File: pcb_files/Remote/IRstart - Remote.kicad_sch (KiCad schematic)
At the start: 32 parts, among them Q1 2N7002, Q2 2N7002, SW1 SW_DIP_x02, SW2 SW_DIP_x02, SW3 SW_DPDT_x2, U2 AP1117-33

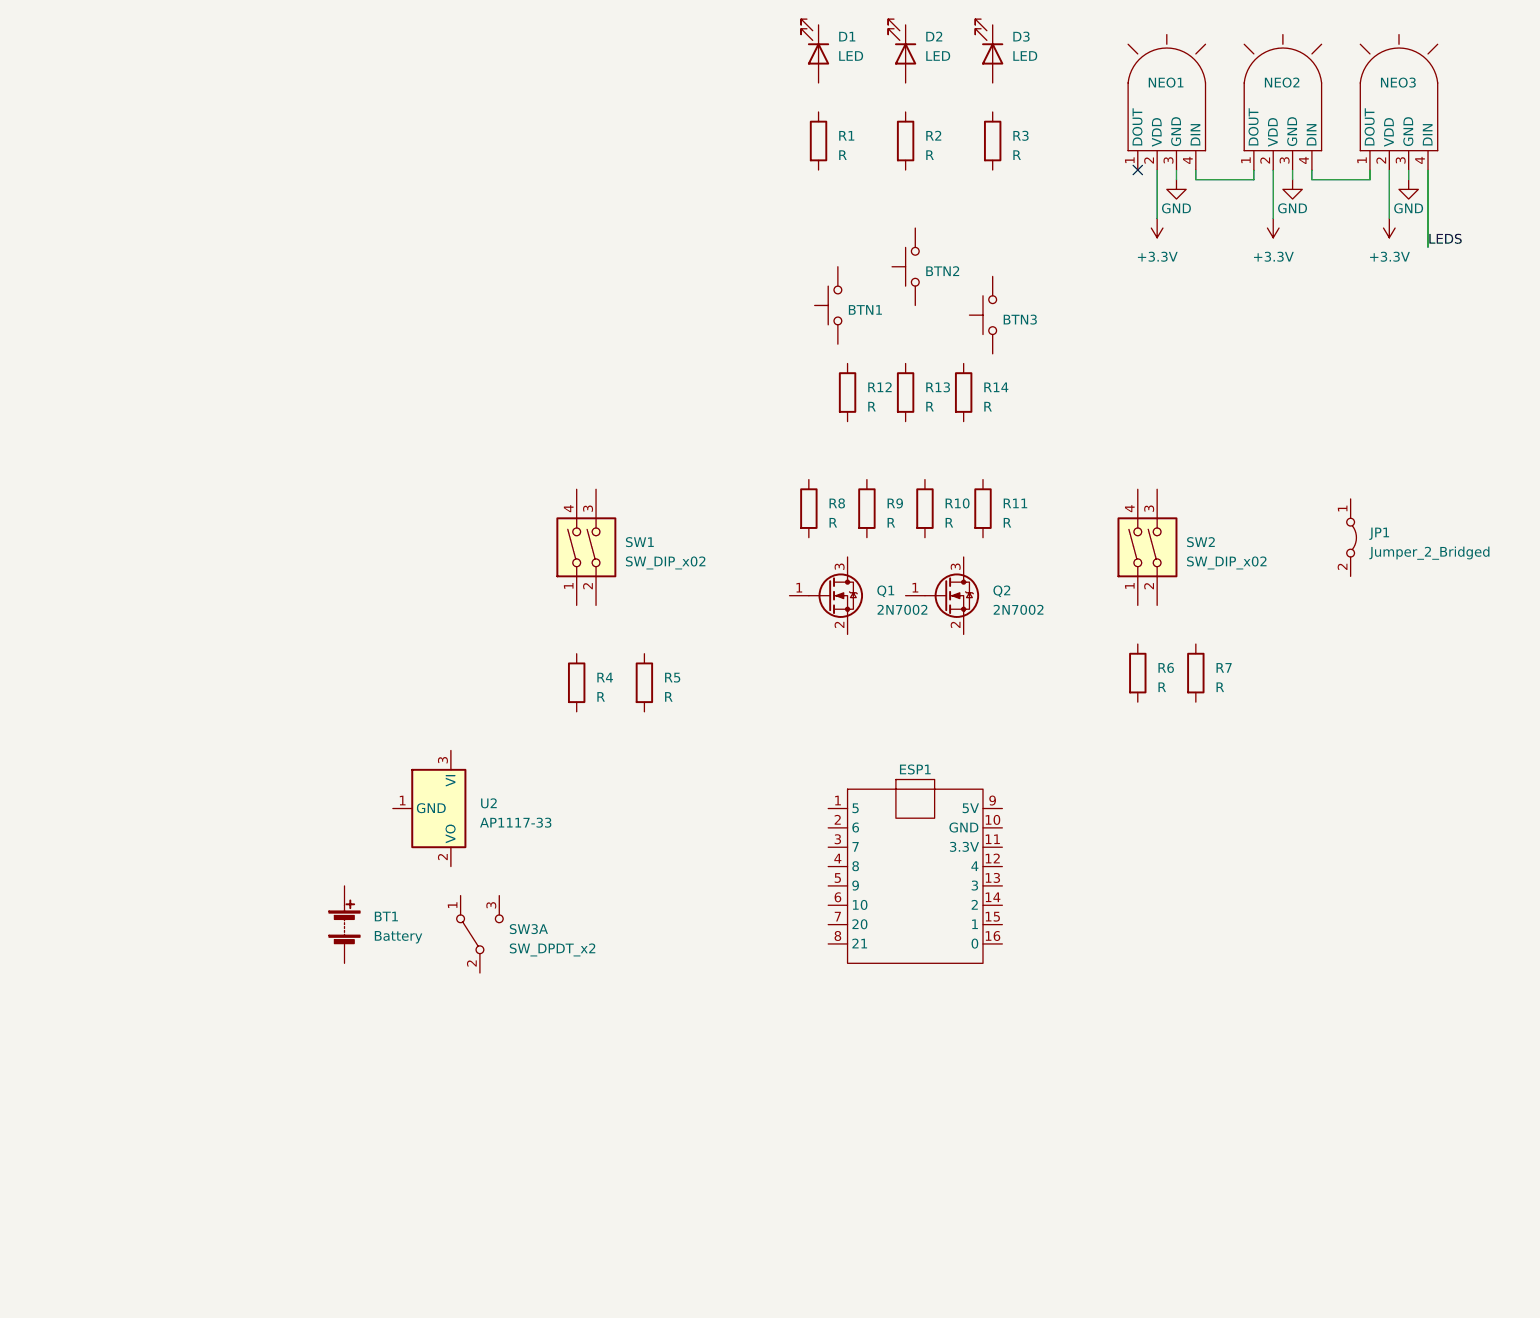
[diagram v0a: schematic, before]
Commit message: Avanza con el diseño del mando. Acaba esquema y ordena componentes PCB
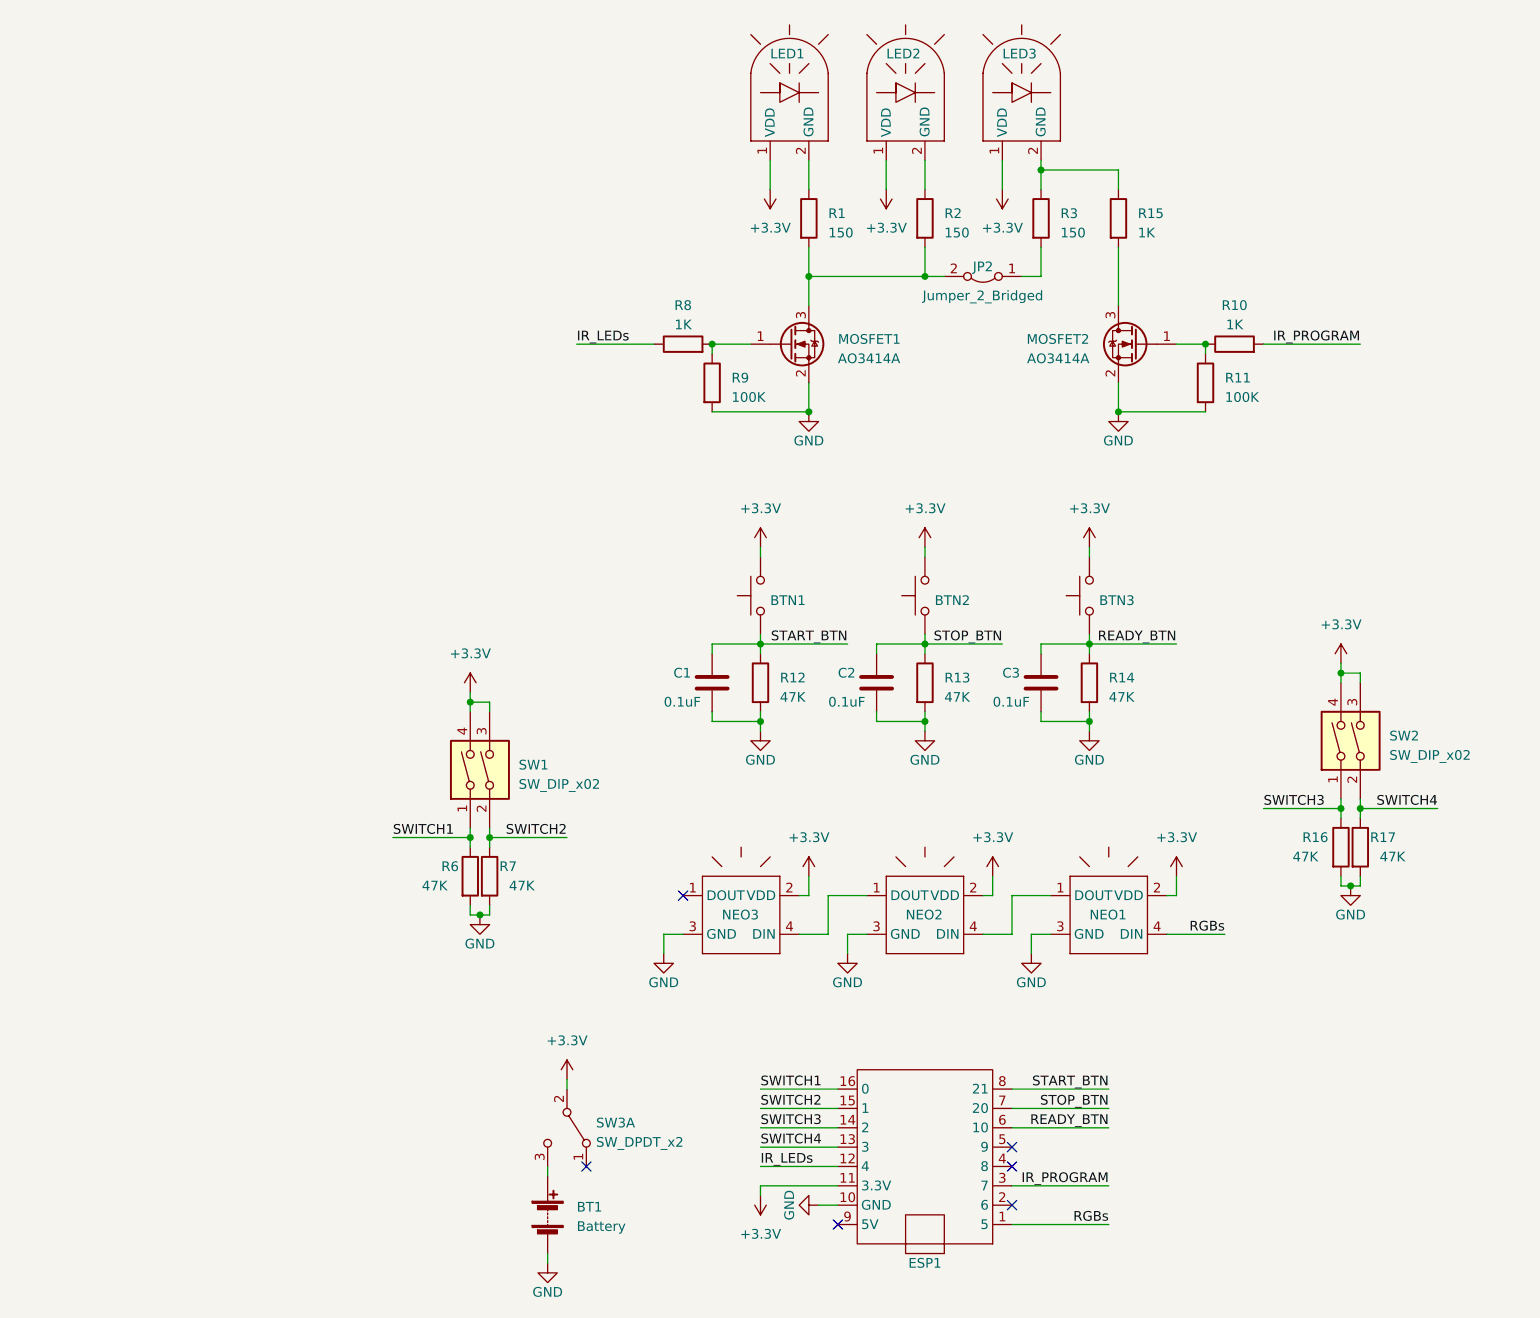
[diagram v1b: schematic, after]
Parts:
- removed D1, D2, D3: LED, symbol Device:LED
- removed JP1: Jumper_2_Bridged, symbol Jumper:Jumper_2_Bridged
- removed Q1, Q2: 2N7002, Package_TO_SOT_SMD:SOT-23, symbol Transistor_FET:2N7002
- removed R4, R5: R, symbol Device:R
- removed U2: AP1117-33, Package_TO_SOT_SMD:SOT-223-3_TabPin2, symbol Regulator_Linear:AP1117-33
- added C1, C2, C3: 0.1uF, Capacitor_SMD:C_0805_2012Metric_Pad1.18x1.45mm_HandSolder, symbol Device:C
- added JP2: Jumper_2_Bridged, Jumper:SolderJumper-2_P1.3mm_Bridged_Pad1.0x1.5mm, symbol Jumper:Jumper_2_Bridged
- added LED2, LED3: ~, LED_SMD:LED_PLCC-2_3x2mm_KA, symbol custom_symbols:Led_5mm_WS2812D_
- added MOSFET1, MOSFET2: AO3414A, Package_TO_SOT_SMD:SOT-23, symbol Transistor_FET:AO3400A
- added NEO2: ~, LED_SMD:LED_WS2812B-2020_PLCC4_2.0x2.0mm, symbol custom_symbols:Led_5mm_WS2812D_
- added R15: 1K, Resistor_SMD:R_0805_2012Metric_Pad1.20x1.40mm_HandSolder, symbol Device:R
- added R16, R17: 47K, Resistor_SMD:R_0805_2012Metric_Pad1.20x1.40mm_HandSolder, symbol Device:R
- BT1: footprint (none) -> Battery:BatteryHolder_Keystone_3002_1x2032; Aliexpress (none) -> https://es.aliexpress.com/item/1005006029630007.html
- BTN1, BTN2, BTN3: footprint (none) -> Button_Switch_SMD:SW_Push_1P1T_NO_6x6mm_H9.5mm; Aliexpress (none) -> https://es.aliexpress.com/item/1005005602103011.html
- ESP1: Aliexpress (none) -> https://es.aliexpress.com/item/1005006350465839.html
- LED1: renamed from NEO2; footprint custom_footprints:LED_D5.0mm-4_RGB_Staggered_Pins -> LED_SMD:LED_PLCC-2_3x2mm_KA; Aliexpress (none) -> https://es.aliexpress.com/item/1005003852381793.html
- NEO1, NEO3: footprint custom_footprints:LED_D5.0mm-4_RGB_Staggered_Pins -> LED_SMD:LED_WS2812B-2020_PLCC4_2.0x2.0mm; Aliexpress (none) -> https://es.aliexpress.com/item/1005006449117605.html
- R1, R2, R3: value R -> 150; footprint (none) -> Resistor_SMD:R_0805_2012Metric_Pad1.20x1.40mm_HandSolder
- R10, R8: value R -> 1K; footprint (none) -> Resistor_SMD:R_0805_2012Metric_Pad1.20x1.40mm_HandSolder
- R11, R9: value R -> 100K; footprint (none) -> Resistor_SMD:R_0805_2012Metric_Pad1.20x1.40mm_HandSolder
- R12, R13, R14, R6, R7: value R -> 47K; footprint (none) -> Resistor_SMD:R_0805_2012Metric_Pad1.20x1.40mm_HandSolder
- SW1, SW2: footprint (none) -> Button_Switch_SMD:SW_DIP_SPSTx02_Slide_6.7x6.64mm_W8.61mm_P2.54mm_LowProfile; Aliexpress (none) -> https://es.aliexpress.com/item/1005006144087226.html
- SW3: footprint (none) -> Button_Switch_SMD:SW_SPDT_PCM12; Aliexpress (none) -> https://es.aliexpress.com/item/32963237441.html
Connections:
- net +3.3V: now also BTN1.2, BTN2.2, BTN3.2, ESP1.11 (3.3V), LED1.1 (VDD), SW1.3, SW1.4, SW2.3, SW2.4, SW3.2 (B), LED2.1 (VDD), LED3.1 (VDD), NEO2.2 (VDD); no longer LED1.2 (VDD)
- net GND: now also BT1.2 (-), ESP1.10 (GND), R11.2, R12.2, R13.2, R14.2, R6.2, R7.2, R9.2, C1.2, C2.2, C3.2, MOSFET1.2 (S), MOSFET2.2 (S), NEO2.3 (GND), R16.2, R17.2; no longer LED1.3 (GND)
- net at R9.1: now also R8.2, MOSFET1.1 (G)
- net START_BTN: now reaches BTN1.1
- net START_BTN: now also ESP1.8 (21), R12.1, C1.1
- net at BT1.1 (+): now also SW3.3 (C)
- net at R1.1: now also LED1.2 (GND)
- net at R1.2: now also R2.2, JP2.2 (B), MOSFET1.3 (D)
- net SWITCH2: now reaches R7.1
- net SWITCH2: now also ESP1.15 (1), SW1.2
- net SWITCH3: now reaches SW2.1
- net SWITCH3: now also ESP1.14 (2), R16.1
- net SWITCH4: now reaches SW2.2
- net SWITCH4: now also ESP1.13 (3), R17.1
- net IR_LEDs: now reaches R8.1
- net IR_LEDs: now also ESP1.12 (4)
- net READY_BTN: now reaches BTN3.1
- net READY_BTN: now also ESP1.6 (10), R14.1, C3.1
- net RGBs: now reaches NEO1.4 (DIN)
- net RGBs: now also ESP1.1 (5); no longer LED1.1 (DOUT)
- net at NEO3.1 (DOUT): no longer LED1.4 (DIN)
- net at R11.1: now also R10.1, MOSFET2.1 (G)
- net SWITCH1: now reaches ESP1.16 (0)
- net SWITCH1: now also R6.1, SW1.1
- net IR_PROGRAM: now reaches ESP1.3 (7)
- net IR_PROGRAM: now also R10.2
- net STOP_BTN: now reaches ESP1.7 (20)
- net STOP_BTN: now also BTN2.1, R13.1, C2.1
- net at R3.1: now also LED3.2 (GND), R15.1
- net at R3.2: now also JP2.1 (A)
- net at NEO1.1 (DOUT): now also NEO2.4 (DIN)
- net at R2.1: now also LED2.2 (GND)
- net LEDS: no longer names the net of NEO3.4 (DIN)
- net LEDS: now also NEO2.1 (DOUT)
- new net: MOSFET2.3 (D), R15.2
- no-connect marks 1 -> 6
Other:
- moved on the sheet: BT1, BTN1, BTN2, BTN3, ESP1, LED1, R10, R11, R12, R13, R14, R6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

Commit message: Avanza con el diseño de la PCB
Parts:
- removed JP2: Jumper_2_Bridged, Jumper:SolderJumper-2_P1.3mm_Bridged_Pad1.0x1.5mm, symbol Jumper:Jumper_2_Bridged
- added C4, C5: 10uF, Capacitor_SMD:C_0805_2012Metric_Pad1.18x1.45mm_HandSolder, symbol Device:C
- added D1, D2: LED, LED_SMD:LED_0805_2012Metric_Pad1.15x1.40mm_HandSolder, symbol Device:LED
- added LDO1: ~, Package_TO_SOT_SMD:SOT-23-5_HandSoldering, symbol custom_symbols:LDO_ME611C33
- added R18: 1K5, Resistor_SMD:R_0805_2012Metric_Pad1.20x1.40mm_HandSolder, symbol Device:R
- added R19: 0, Resistor_SMD:R_0805_2012Metric_Pad1.20x1.40mm_HandSolder, symbol Device:R
- added R4, R5: 1K, Resistor_SMD:R_0805_2012Metric_Pad1.20x1.40mm_HandSolder, symbol Device:R
- added TP4056: ~, Package_SO:SOP-8_3.9x4.9mm_P1.27mm, symbol custom_symbols:4056H
- BT1: footprint Battery:BatteryHolder_Keystone_3002_1x2032 -> custom_footprints:Leds_IR_Remote; Aliexpress https://es.aliexpress.com/item/1005006029630007.html -> https://es.aliexpress.com/item/1005006776171377.html
- LED1: footprint LED_SMD:LED_PLCC-2_3x2mm_KA -> custom_footprints:Leds_IR_Remote
- LED2: renamed from LED3; footprint LED_SMD:LED_PLCC-2_3x2mm_KA -> custom_footprints:Leds_IR_Remote
- LED3: renamed from LED2; footprint LED_SMD:LED_PLCC-2_3x2mm_KA -> custom_footprints:Leds_IR_Remote
- NEO1, NEO2, NEO3: footprint LED_SMD:LED_WS2812B-2020_PLCC4_2.0x2.0mm -> custom_footprints:LED_WS2812B_2.0x2.0mm
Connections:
- net +3.3V: now also LDO1.5 (VOUT); no longer SW3.2 (B)
- net GND: now also C4.2, C5.2, LDO1.2 (VSS), R18.2, TP4056.1 (TEMP), TP4056.3 (VSS)
- net at R3.2: now also R19.1
- net at MOSFET1.3 (D), R1.2, R2.2: now also R19.2
- net at SW3.3 (C): no longer BT1.1 (+)
- net BATT: now reaches SW3.1 (A)
- net BATT: now also BT1.1 (+), C5.1, TP4056.5 (BAT)
- net +5V: now reaches ESP1.9 (5V)
- net +5V: now also C4.1, R4.1, R5.1, TP4056.4 (VIN), TP4056.8 (EN)
- new net: LDO1.1 (VIN), LDO1.3 (CE), SW3.2 (B)
- new net: R18.1, TP4056.2 (ISET)
- new net: D1.2 (A), R4.2
- new net: D2.2 (A), R5.2
- new net LED_CARGA: D1.1 (K), TP4056.7 (STAT1)
- new net LED_CARGADO: D2.1 (K), TP4056.6 (STAT2)
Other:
- moved on the sheet: BTN1, BTN2, BTN3, C1, C2, C3, LED1, LED2, LED3, MOSFET1, MOSFET2, NEO1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
